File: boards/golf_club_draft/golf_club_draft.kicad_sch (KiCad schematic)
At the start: 20 parts, among them J1 USB_C_Receptacle_USB2.0_16P, Q1 PNP, U1 MPU-9250

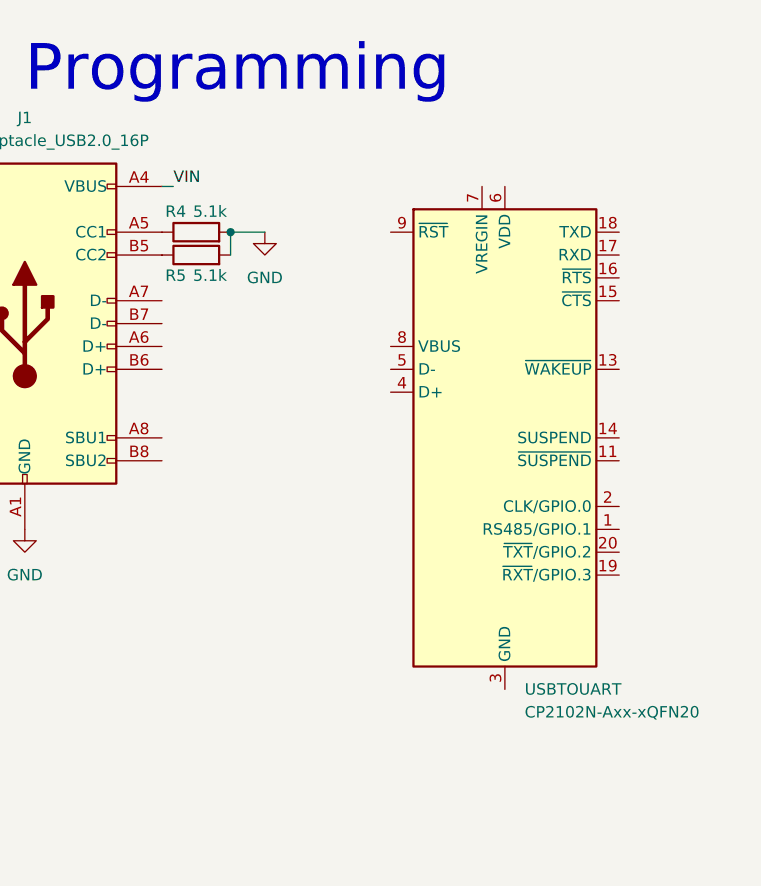
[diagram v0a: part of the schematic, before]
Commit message: Continued programming circuit (Through USBC)
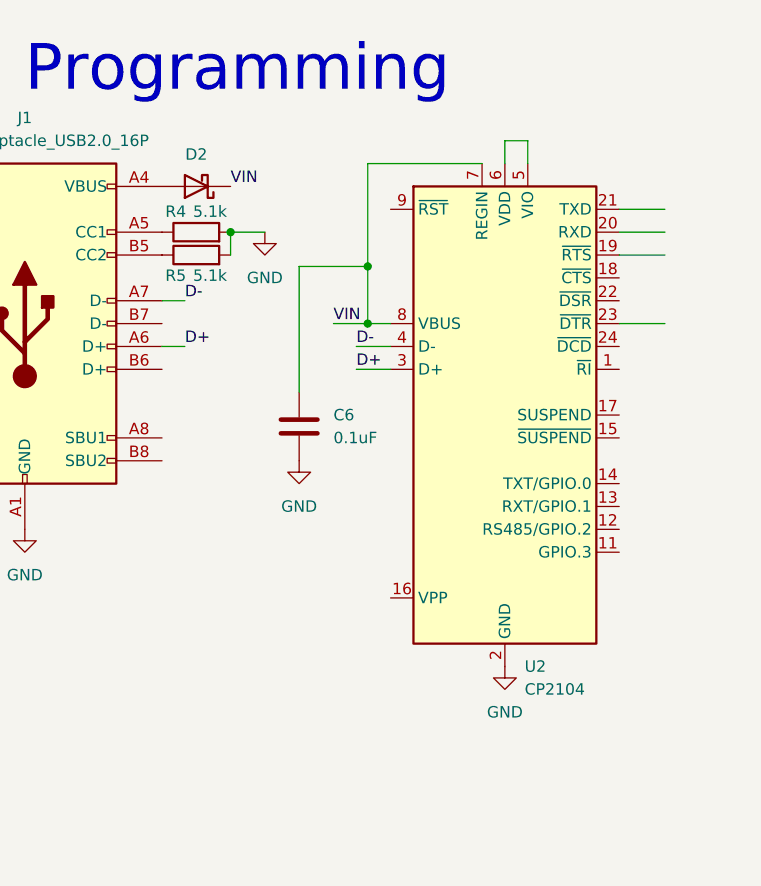
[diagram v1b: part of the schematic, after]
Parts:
- removed USBTOUART: CP2102N-Axx-xQFN20, Package_DFN_QFN:SiliconLabs_QFN-20-1EP_3x3mm_P0.5mm, symbol Interface_USB:CP2102N-Axx-xQFN20
- added C6: 0.1uF, symbol Device:C
- added D2: D_Schottky, symbol Device:D_Schottky
- added U2: CP2104, Package_DFN_QFN:QFN-24-1EP_4x4mm_P0.5mm_EP2.6x2.6mm, symbol Interface_USB:CP2104
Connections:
- net GND: now also C6.2, U2.2 (GND), U2.25 (GND)
- net VIN: now also C6.1, D2.1 (K), U2.7 (REGIN), U2.8 (VBUS); no longer J1.A4 (VBUS), J1.A9 (VBUS), J1.B4 (VBUS), J1.B9 (VBUS)
- net D+: now reaches J1.A6 (D+)
- net D+: now also U2.3 (D+)
- net D-: now reaches J1.A7 (D-)
- net D-: now also U2.4 (D-)
- new net: D2.2 (A), J1.A4 (VBUS), J1.A9 (VBUS), J1.B4 (VBUS), J1.B9 (VBUS)
- new net: U2.5 (VIO), U2.6 (VDD)

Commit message: Finalized first draft of schematic
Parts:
- removed 2V5LR1: AZ1117-2.5, symbol Regulator_Linear:AZ1117-2.5
- removed ESP32MC1: ESP32-S3-WROOM-2, RF_Module:ESP32-S3-WROOM-2, symbol RF_Module:ESP32-S3-WROOM-2
- removed U1: MPU-9250, Sensor_Motion:InvenSense_QFN-24_3x3mm_P0.4mm, symbol Sensor_Motion:MPU-9250
- added 1V8LR1: AZ1117-1.8, symbol Regulator_Linear:AZ1117-1.8
- added C10, C11, C9: 0.1uF, Capacitor_SMD:C_0805_2012Metric_Pad1.18x1.45mm_HandSolder, symbol Device:C
- added C7, C8: 1uF, Capacitor_SMD:C_0805_2012Metric_Pad1.18x1.45mm_HandSolder, symbol Device:C
- added FSR_IO, FSR_V: Conn_01x04_Socket, symbol Connector:Conn_01x04_Socket
- added IMU_IO: Conn_01x05_Socket, symbol Connector:Conn_01x05_Socket
- added Q2: NPN, symbol Simulation_SPICE:NPN
- added Q3: PNP, symbol Simulation_SPICE:PNP
- added R6, R7, R8, R9: 10K, symbol Device:R
- added U1: ICM-20948, Sensor_Motion:InvenSense_QFN-24_3x3mm_P0.4mm, symbol Sensor_Motion:ICM-20948
- added U3: ESP32-S3-WROOM-1, RF_Module:ESP32-S3-WROOM-1, symbol RF_Module:ESP32-S3-WROOM-1
- C1, C3: value C -> 10uF; footprint (none) -> Capacitor_SMD:C_0805_2012Metric_Pad1.18x1.45mm_HandSolder
- C2, C4: value C -> 22uF; footprint (none) -> Capacitor_SMD:C_0805_2012Metric_Pad1.18x1.45mm_HandSolder
- C5, C6: footprint (none) -> Capacitor_SMD:C_0805_2012Metric_Pad1.18x1.45mm_HandSolder
- renumbered BATTCHARGER to BATTCHARGER1, BATTIO to BATTIO1
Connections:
- net 3V3: now also C10.1, FSR_V.1 (Pin_1), FSR_V.2 (Pin_2), FSR_V.3 (Pin_3), FSR_V.4 (Pin_4), IMU_IO.1 (Pin_1), U1.13 (VDD), U3.2 (3V3)
- net GND: now also 1V8LR1.1 (GND), C10.2, C11.2, C7.1, C8.1, C9.1, IMU_IO.4 (Pin_4), R6.1, R7.1, R8.1, R9.1, U1.18 (GND), U1.20 (GND), U3.1 (GND), U3.40 (GND), U3.41 (GND)
- net VBATT: now also 1V8LR1.3 (VI)
- net RTS: now reaches U2.19 (~{RTS})
- net RTS: now also Q2.3 (E), Q3.2 (B)
- net RXD: now reaches U2.20 (RXD)
- net RXD: now also U3.36 (RXD0)
- net TXD: now reaches U2.21 (TXD)
- net TXD: now also U3.37 (TXD0)
- net DTR: now reaches U2.23 (~{DTR})
- net DTR: now also Q2.2 (B), Q3.3 (E)
- net 2V5 renamed 1V8
- net 1V8: now also 1V8LR1.2 (VO), C9.2, IMU_IO.5 (Pin_5), U1.8 (VDDIO)
- new net: C11.1, U1.10 (REGOUT)
- new net FSR1: FSR_IO.1 (Pin_1), R6.2, U3.4 (IO4)
- new net FSR2: FSR_IO.2 (Pin_2), R7.2, U3.5 (IO5)
- new net FSR3: FSR_IO.3 (Pin_3), R8.2, U3.6 (IO6)
- new net FSR4: FSR_IO.4 (Pin_4), R9.2, U3.7 (IO7)
- new net GPIO0: Q3.1 (C), U3.27 (IO0)
- new net RESET: C7.2, C8.2, Q2.1 (C), U3.3 (EN)
- new net SCL: IMU_IO.3 (Pin_3), U1.23 (SCL/SCLK), U3.20 (IO12)
- new net SDA: IMU_IO.2 (Pin_2), U1.24 (SDA/SDI), U3.19 (IO11)
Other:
- added sheet positional_sensor (positional_sensor.kicad_sch)

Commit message: one more commit for final first draft of schematic
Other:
- note added: "IMU"
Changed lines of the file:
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@@
+		)
+	)
+	(text "IMU"
+		(exclude_from_sim no)
+		(at 410.972 7.112 0)
+		(effects
+			(font
+				(size 5.08 5.08)
+			)
 		)
 	)
